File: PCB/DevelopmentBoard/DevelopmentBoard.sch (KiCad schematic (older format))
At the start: 27 parts, among them J2 Conn_01x04_MountingPin-Payloa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, J5 Conn_01x04_MountingPin, U1 D24V22F5_VoltageRegulator, U2 Barometer_Grove, U3 RASPBERRY_PI_3_MODEL_B+, U4 Conn_01x08_DevBoardSymbols, U6 MCP3008_ADC, U7 Conn_01x06_DevBoard_Symbols, X1 XT30, X2 XT30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

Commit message: Rewired I2C Pins on the Pi
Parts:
- gave numbers to parts that had none: 1
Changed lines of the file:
@@
 	5000 10000 9000 10000
 Wire Wire Line
+	7750 10850 8000 10850
+Wire Wire Line
 	7750 10750 8000 10750
-Wire Wire Line
-	7750 10850 8000 10850
+Text Label 8000 10850 2    50   ~ 0
+SDA
 Text Label 8000 10750 2    50   ~ 0
-SDA
-Text Label 8000 10850 2    50   ~ 0
 SCL
 $Comp
@@
 Text Label 1150 17900 1    50   ~ 0
 CS_ADC
-Text Label 1800 4350 0    50   ~ 0
+Text Label 1800 2550 0    50   ~ 0
 SCL
-Text Label 1800 4250 0    50   ~ 0
+Text Label 1800 2450 0    50   ~ 0
 SDA
 Wire Wire Line
-	1950 4350 1750 4350
-Wire Wire Line
-	1950 4250 1750 4250
+	1950 2550 1750 2550
+Wire Wire Line
+	1950 2450 1750 2450
 $Comp
 L power:+5V #PWR0116
@@
 $EndComp
 $Comp
-L Connector:TestPoint TP?
+L Connector:TestPoint TP2
 U 1 1 623429F1
 P 1100 15350
-F 0 "TP?" H 1158 15468 50  0000 L CNN
+F 0 "TP2" H 1158 15468 50  0000 L CNN
 F 1 "TestPoint" H 1158 15377 50  0000 L CNN
 F 2 "TestPoint:TestPoint_Pad_D2.5mm" H 1300 15350 50  0001 C CNN
@@
 $EndComp
 $Comp
-L power:+3V3 #PWR?
+L power:+3V3 #PWR0120
 U 1 1 623433B8
 P 1100 15350
-F 0 "#PWR?" H 1100 15200 50  0001 C CNN
+F 0 "#PWR0120" H 1100 15200 50  0001 C CNN
 F 1 "+3V3" H 1115 15523 50  0000 C CNN
 F 2 "" H 1100 15350 50  0001 C CNN

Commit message: Added I2C Outputs on the TBS Module
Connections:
- wire segments 60 -> 62
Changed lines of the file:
@@
 U 1 1 617175F8
 P 1600 15250
-F 0 "X1" H 1800 15350 50  0000 C CNN
-F 1 "XT30" H 1850 15250 50  0000 C CNN
+F 0 "X1" H 1900 15450 50  0000 C CNN
+F 1 "XT30" H 2000 15100 50  0000 C CNN
 F 2 "Connector_AMASS:AMASS_XT30U-M_1x02_P5.0mm_Vertical" H 1550 15250 50  0001 C CNN
 F 3 "" H 1550 15250 50  0001 C CNN
@@
 P 1100 15350
 F 0 "TP2" H 1158 15468 50  0000 L CNN
-F 1 "TestPoint" H 1158 15377 50  0000 L CNN
+F 1 "TestPoint" H 1150 15400 50  0000 L CNN
 F 2 "TestPoint:TestPoint_Pad_D2.5mm" H 1300 15350 50  0001 C CNN
 F 3 "~" H 1300 15350 50  0001 C CNN
@@
 	-1   0    0    1
 $EndComp
+Text Label 3450 15800 0    50   ~ 0
+SCL
+Text Label 3450 15700 0    50   ~ 0
+SDA
+Wire Wire Line
+	3600 15800 3400 15800
+Wire Wire Line
+	3600 15700 3400 15700
 $EndSCHEMATC

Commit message: FInal Tracing changes and Copper Refill.
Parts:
- renumbered R20 to R5
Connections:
- wire segments 62 -> 65
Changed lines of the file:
@@
 CS_ADC
 $Comp
-L Connector:TestPoint TP1
-U 1 1 626A437A
-P 2400 15250
-F 0 "TP1" H 2458 15368 50  0000 L CNN
-F 1 "TestPoint" H 2458 15277 50  0000 L CNN
-F 2 "TestPoint:TestPoint_Pad_D2.5mm" H 2600 15250 50  0001 C CNN
-F 3 "~" H 2600 15250 50  0001 C CNN
-	1    2400 15250
-	1    0    0    -1
-$EndComp
-$Comp
-L power:+12V #PWR0114
-U 1 1 626A5499
-P 2400 15250
-F 0 "#PWR0114" H 2400 15100 50  0001 C CNN
-F 1 "+12V" H 2415 15423 50  0000 C CNN
-F 2 "" H 2400 15250 50  0001 C CNN
-F 3 "" H 2400 15250 50  0001 C CNN
-	1    2400 15250
-	-1   0    0    1
-$EndComp
-$Comp
-L Device:R_Small_US R20
+L Device:R_Small_US R5
 U 1 1 626DE972
 P 1150 17100
-F 0 "R20" H 1218 17146 50  0000 L CNN
+F 0 "R5" H 1218 17146 50  0000 L CNN
 F 1 "4.7k" H 1218 17055 50  0000 L CNN
 F 2 "DevelopmentBoard:0603" H 1150 17100 50  0001 C CNN
@@
 Wire Wire Line
 	3600 15700 3400 15700
+$Comp
+L Connector:TestPoint TP1
+U 1 1 626A437A
+P 2400 15250
+F 0 "TP1" H 2458 15368 50  0000 L CNN
+F 1 "TestPoint" H 2458 15277 50  0000 L CNN
+F 2 "TestPoint:TestPoint_Pad_D2.5mm" H 2600 15250 50  0001 C CNN
+F 3 "~" H 2600 15250 50  0001 C CNN
+	1    2400 15250
+	1    0    0    -1
+$EndComp
+Wire Wire Line
+	2400 15250 2400 15400
+Wire Wire Line
+	2400 15400 2050 15400
+Wire Wire Line
+	2050 15400 2050 15700
+Connection ~ 2050 15700
 $EndSCHEMATC

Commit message: Added regulator symbols
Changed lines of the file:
@@
 	1000 22500 1000 1000
 Wire Notes Line
-	700  950  8700 950
+	1000 975  9000 975
 Wire Notes Line
 	9000 1000 9000 22500

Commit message: Added NAV route to breakout
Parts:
- added U?: VN-100_Breakout, symbol DevelopmentBoard:VN-100_Breakout
- R1, R11, R12, R13, R14, R15, R2, R3, R4, R5, R6: symbol Device:R_Small_US -> DevelopmentBoard-rescue:R_Small_US-Device
- TP1, TP2, TP3, TP4: symbol Connector:TestPoint -> DevelopmentBoard-rescue:TestPoint-Connector
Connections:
- net labels added: +5V-power, GND-power, NAV_RX, NAV_TX
- wire segments 65 -> 74
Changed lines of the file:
@@
 $EndDescr
 $Comp
-L power:GND #PWR0164
+L DevelopmentBoard-rescue:GND-power #PWR0164
 U 1 1 61619131
 P 4400 15500
@@
 $EndComp
 $Comp
-L power:+5V #PWR0165
+L DevelopmentBoard-rescue:+5V-power #PWR0165
 U 1 1 6161BA5A
 P 4400 15600
@@
 $EndComp
 $Comp
-L power:GND #PWR0166
+L DevelopmentBoard-rescue:GND-power #PWR0166
 U 1 1 61656710
 P 1850 15200
@@
 $EndComp
 $Comp
-L power:+12V #PWR0167
+L DevelopmentBoard-rescue:+12V-power #PWR0167
 U 1 1 61660D0C
 P 1850 15300
@@
 	1750 15300 1850 15300
 $Comp
-L power:GND #PWR0168
+L DevelopmentBoard-rescue:GND-power #PWR0168
 U 1 1 6161AEF3
 P 3600 15600
@@
 	3400 17300 3050 17300
 $Comp
-L power:GND #PWR0171
+L DevelopmentBoard-rescue:GND-power #PWR0171
 U 1 1 616717DD
 P 3400 17100
@@
 $EndComp
 $Comp
-L power:+5V #PWR0172
+L DevelopmentBoard-rescue:+5V-power #PWR0172
 U 1 1 6167029D
 P 3400 17200
@@
 $EndComp
 $Comp
-L power:+3.3V #PWR0177
+L DevelopmentBoard-rescue:+3.3V-power #PWR0177
 U 1 1 6160D985
 P 2000 17000
@@
 $EndComp
 $Comp
-L power:+3.3V #PWR0178
+L DevelopmentBoard-rescue:+3.3V-power #PWR0178
 U 1 1 6160D97F
 P 1600 17000
@@
 $EndComp
 $Comp
-L Device:R_Small_US R1
+L DevelopmentBoard-rescue:R_Small_US-Device R1
 U 1 1 6160D96F
 P 1600 17100
@@
 $EndComp
 $Comp
-L Device:R_Small_US R3
+L DevelopmentBoard-rescue:R_Small_US-Device R3
 U 1 1 6160D975
 P 2000 17100
@@
 SCL
 $Comp
-L power:+5V #PWR0208
+L DevelopmentBoard-rescue:+5V-power #PWR0208
 U 1 1 61DC74CC
 P 7750 10950
@@
 $EndComp
 $Comp
-L power:GND #PWR0207
+L DevelopmentBoard-rescue:GND-power #PWR0207
 U 1 1 61DC5E51
 P 7750 11050
@@
 	1750 15700 2050 15700
 $Comp
-L power:GND #PWR0101
+L DevelopmentBoard-rescue:GND-power #PWR0101
 U 1 1 6235DC57
 P 2200 15850
@@
 $EndComp
 $Comp
-L power:GND #PWR0102
+L DevelopmentBoard-rescue:GND-power #PWR0102
 U 1 1 6236A06D
 P 2200 15950
@@
 $EndComp
 $Comp
-L power:+5V #PWR0103
+L DevelopmentBoard-rescue:+5V-power #PWR0103
 U 1 1 62384BC7
 P 2250 16050
@@
 	7900 2550 8100 2550
 $Comp
-L power:GND #PWR0106
+L DevelopmentBoard-rescue:GND-power #PWR0106
 U 1 1 62490609
 P 8100 2550
@@
 $EndComp
 $Comp
-L power:GND #PWR0107
+L DevelopmentBoard-rescue:GND-power #PWR0107
 U 1 1 6249144C
 P 8250 3050
@@
 	1600 3650 1950 3650
 $Comp
-L Device:R_Small_US R2
+L DevelopmentBoard-rescue:R_Small_US-Device R2
 U 1 1 624B7DEB
 P 6650 2350
@@
 $EndComp
 $Comp
-L Device:R_Small_US R4
+L DevelopmentBoard-rescue:R_Small_US-Device R4
 U 1 1 624BB4C6
 P 6650 2450
@@
 $EndComp
 $Comp
-L Device:R_Small_US R6
+L DevelopmentBoard-rescue:R_Small_US-Device R6
 U 1 1 624BDAC4
 P 6650 2550
@@
 $EndComp
 $Comp
-L Device:R_Small_US R11
+L DevelopmentBoard-rescue:R_Small_US-Device R11
 U 1 1 624BE5AF
 P 6650 2650
@@
 $EndComp
 $Comp
-L Device:R_Small_US R12
+L DevelopmentBoard-rescue:R_Small_US-Device R12
 U 1 1 624BF3CC
 P 6650 2750
@@
 $EndComp
 $Comp
-L Device:R_Small_US R13
+L DevelopmentBoard-rescue:R_Small_US-Device R13
 U 1 1 624BFB63
 P 6650 2850
@@
 $EndComp
 $Comp
-L Device:R_Small_US R14
+L DevelopmentBoard-rescue:R_Small_US-Device R14
 U 1 1 624C06DD
 P 6650 2950
@@
 $EndComp
 $Comp
-L Device:R_Small_US R15
+L DevelopmentBoard-rescue:R_Small_US-Device R15
 U 1 1 624C10BC
 P 6650 3050
@@
 	6250 3050 6550 3050
 $Comp
-L Connector:TestPoint TP4
+L DevelopmentBoard-rescue:TestPoint-Connector TP4
 U 1 1 62563BD3
 P 1550 16050
@@
 $EndComp
 $Comp
-L power:+5V #PWR0108
+L DevelopmentBoard-rescue:+5V-power #PWR0108
 U 1 1 62568910
 P 1550 16050
@@
 $EndComp
 $Comp
-L Connector:TestPoint TP3
+L DevelopmentBoard-rescue:TestPoint-Connector TP3
 U 1 1 6256C309
 P 1100 16050
@@
 $EndComp
 $Comp
-L power:GND #PWR0109
+L DevelopmentBoard-rescue:GND-power #PWR0109
 U 1 1 6256D475
 P 1100 16050
@@
 	6200 11750 6400 11750
 $Comp
-L power:GND #PWR0110
+L DevelopmentBoard-rescue:GND-power #PWR0110
 U 1 1 62628D89
 P 6200 11950
@@
 $EndComp
 $Comp
-L power:+5V #PWR0111
+L DevelopmentBoard-rescue:+5V-power #PWR0111
 U 1 1 62629E2C
 P 6200 11850
@@
 $EndComp
 $Comp
-L power:+5V #PWR0112
+L DevelopmentBoard-rescue:+5V-power #PWR0112
 U 1 1 626358DD
 P 7850 12050
@@
 $EndComp
 $Comp
-L power:GND #PWR0113
+L DevelopmentBoard-rescue:GND-power #PWR0113
 U 1 1 6263718E
 P 7850 12150
@@
 CS_ADC
 $Comp
-L Device:R_Small_US R5
+L DevelopmentBoard-rescue:R_Small_US-Device R5
 U 1 1 626DE972
 P 1150 17100
@@
 $EndComp
 $Comp
-L power:+3.3V #PWR0115
+L DevelopmentBoard-rescue:+3.3V-power #PWR0115
 U 1 1 626DFEE0
 P 1150 17000
@@
 	1950 2450 1750 2450
 $Comp
-L power:+5V #PWR0116
+L DevelopmentBoard-rescue:+5V-power #PWR0116
 U 1 1 623DD84B
 P 4050 2350
@@
 $EndComp
 $Comp
-L power:+3.3V #PWR0117
+L DevelopmentBoard-rescue:+3.3V-power #PWR0117
 U 1 1 62402BAE
 P 4050 2450
@@
 	7900 2750 8250 2750
 $Comp
-L power:+5V #PWR0104
+L DevelopmentBoard-rescue:+5V-power #PWR0104
 U 1 1 6232D937
 P 8100 2350
@@
 $EndComp
 $Comp
-L power:+5V #PWR0105
+L DevelopmentBoard-rescue:+5V-power #PWR0105
 U 1 1 6232E513
 P 8100 2450
@@
 $EndComp
 $Comp
-L power:GND #PWR0118
+L DevelopmentBoard-rescue:GND-power #PWR0118
 U 1 1 62355844
 P 4050 4550
@@
 $EndComp
 $Comp
-L power:GND #PWR0119
+L DevelopmentBoard-rescue:GND-power #PWR0119
 U 1 1 62356241
 P 4050 4450
@@
 $EndComp
 $Comp
-L Connector:TestPoint TP2
+L DevelopmentBoard-rescue:TestPoint-Connector TP2
 U 1 1 623429F1
 P 1100 15350
@@
 $EndComp
 $Comp
-L power:+3V3 #PWR0120
+L DevelopmentBoard-rescue:+3V3-power #PWR0120
 U 1 1 623433B8
 P 1100 15350
@@
 	3600 15700 3400 15700
 $Comp
-L Connector:TestPoint TP1
+L DevelopmentBoard-rescue:TestPoint-Connector TP1
 U 1 1 626A437A
 P 2400 15250
@@
 	2050 15400 2050 15700
 Connection ~ 2050 15700
+$Comp
+L DevelopmentBoard:VN-100_Breakout U?
+U 1 1 625A78A9
+P 2950 9650
+F 0 "U?" H 2950 10415 50  0000 C CNN
+F 1 "VN-100_Breakout" H 2950 10324 50  0000 C CNN
+F 2 "" H 3000 9950 50  0001 C CNN
+F 3 "" H 3000 9950 50  0001 C CNN
+	1    2950 9650
+	1    0    0    -1
+$EndComp
+$Comp
+L DevelopmentBoard-rescue:+5V-power #PWR?
+U 1 1 625ABE16
+P 3650 9300
+F 0 "#PWR?" H 3650 9150 50  0001 C CNN
+F 1 "+5V-power" H 3665 9473 50  0000 C CNN
+F 2 "" H 3650 9300 50  0001 C CNN
+F 3 "" H 3650 9300 50  0001 C CNN
+	1    3650 9300
+	1    0    0    -1
+$EndComp
+Wire Wire Line
+	3400 9300 3650 9300
+$Comp
+L DevelopmentBoard-rescue:GND-power #PWR?
+U 1 1 625B8F57
+P 3400 10200
+F 0 "#PWR?" H 3400 9950 50  0001 C CNN
+F 1 "GND-power" H 3405 10027 50  0000 C CNN
+F 2 "" H 3400 10200 50  0001 C CNN
+F 3 "" H 3400 10200 50  0001 C CNN
+	1    3400 10200
+	1    0    0    -1
+$EndComp
+Wire Wire Line
+	3400 10050 3400 10200
+Connection ~ 3400 10200
+Wire Wire Line
+	2500 9450 2300 9450
+Text Label 2300 9450 0    50   ~ 0
+SCLK
+Wire Wire Line
+	2500 9600 2300 9600
+Text Label 2300 9600 0    50   ~ 0
+MOSI
+Wire Wire Line
+	2500 9750 2300 9750
+Text Label 2300 9750 0    50   ~ 0
+MISO
+Text Label 4350 2650 2    50   ~ 0
+NAV_RX
+Wire Wire Line
+	4050 2750 4350 2750
+Wire Wire Line
+	4050 2650 4350 2650
+Text Label 4350 2750 2    50   ~ 0
+NAV_TX
+Wire Wire Line
+	3400 9900 3700 9900
+Text Label 3700 9750 2    50   ~ 0
+NAV_TX
+Wire Wire Line
+	3400 9750 3700 9750
+Text Label 3700 9900 2    50   ~ 0
+NAV_RX
 $EndSCHEMATC

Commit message: initial board layout and traces
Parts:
- removed J2: Conn_01x04_MountingPin-PayloadSymbols, Connector_PinHeader_2.54mm:PinHeader_1x04_P2.54mm_Vertical, symbol DevelopmentBoard-rescue:Conn_01x04_MountingPin-PayloadSymbols
- removed R11, R12, R13, R14, R15, R2, R4, R6: 0, DevelopmentBoard:0603, symbol DevelopmentBoard-rescue:R_Small_US-Device
- removed R5: 4.7k, DevelopmentBoard:0603, symbol DevelopmentBoard-rescue:R_Small_US-Device
- removed U2: Barometer_Grove, DevelopmentBoard:Barometer_Grove, symbol DevelopmentBoard-rescue:Barometer_Grove-PayloadSymbols
- removed U6: MCP3008_ADC, DevelopmentBoard:MCP3008_ADC, symbol DevelopmentBoard:MCP3008_ADC
- removed X3: 2mmGrove_Connector, DevelopmentBoard:2mmGrove_Connector, symbol DevelopmentBoard:2mmGrove_Connector
- added R10, R11, R12, R2, R4, R5, R6, R7, R8, R9: 0, DevelopmentBoard:0603, symbol Device:R_Small_US
- U2: renamed from U?; footprint (none) -> DevelopmentBoard:VN-100Breakout
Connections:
- net labels added: SPI_CS
- net labels removed: CS_ADC
- wire segments 74 -> 56
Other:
- note added: "I2C Pullups"
- note removed: "ADC"
- note removed: "Altimeter"
- note removed: "SPI and I2C Pullups"
- note removed: "USB Controller"
- note removed: "USB Ports"
- moved on the sheet: J5

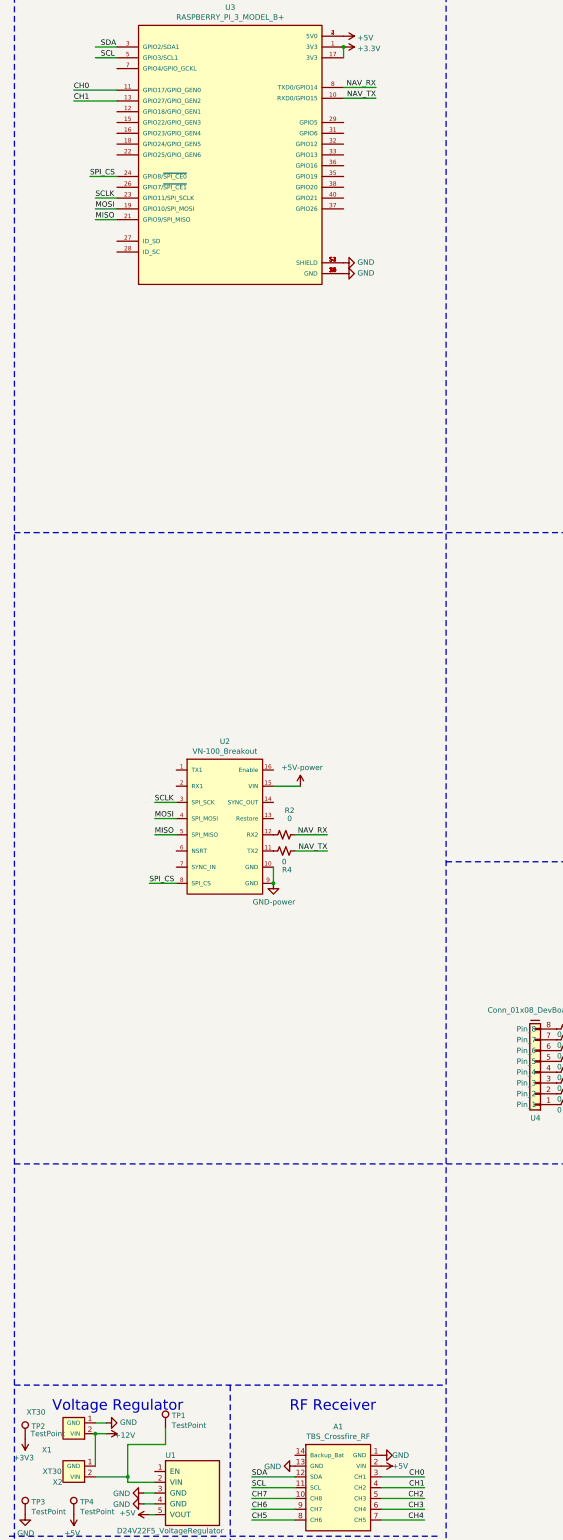
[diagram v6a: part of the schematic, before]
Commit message: Routed TBS connector
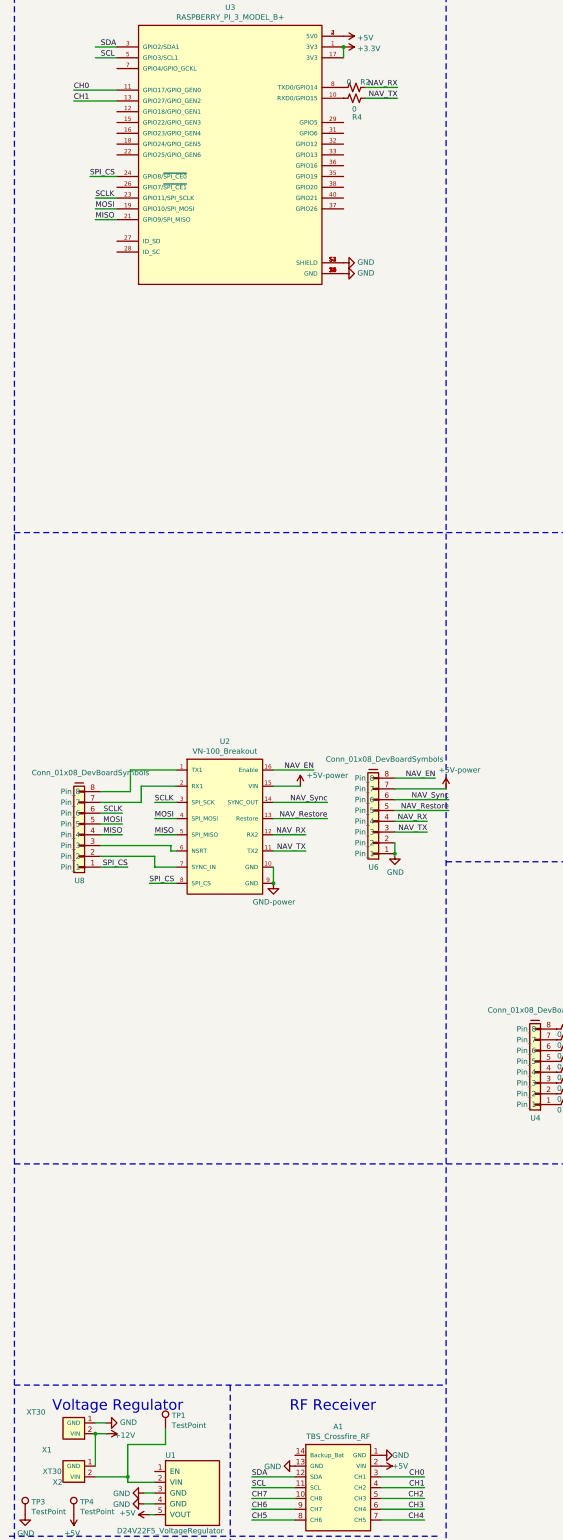
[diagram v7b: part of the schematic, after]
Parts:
- removed TP2: TestPoint, TestPoint:TestPoint_Pad_D2.5mm, symbol DevelopmentBoard-rescue:TestPoint-Connector
- added U6, U8: Conn_01x08_DevBoardSymbols, Connector_PinHeader_2.54mm:PinHeader_1x08_P2.54mm_Vertical, symbol DevelopmentBoard:Conn_01x08_DevBoardSymbols
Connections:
- net labels added: NAV_EN, NAV_Restore, NAV_Sync
- net labels removed: +3V3
- wire segments 56 -> 82
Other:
- moved on the sheet: R2, R4
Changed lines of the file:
@@
 	0    -1   -1   0
-$EndComp
-$Comp
-L DevelopmentBoard-rescue:TestPoint-Connector TP2
-U 1 1 623429F1
-P 1100 15350
-F 0 "TP2" H 1158 15468 50  0000 L CNN
-F 1 "TestPoint" H 1150 15400 50  0000 L CNN
-F 2 "TestPoint:TestPoint_Pad_D2.5mm" H 1300 15350 50  0001 C CNN
-F 3 "~" H 1300 15350 50  0001 C CNN
-	1    1100 15350
-	1    0    0    -1
-$EndComp
-$Comp
-L DevelopmentBoard-rescue:+3V3-power #PWR0120
-U 1 1 623433B8
-P 1100 15350
-F 0 "#PWR0120" H 1100 15200 50  0001 C CNN
-F 1 "+3V3" H 1115 15523 50  0000 C CNN
-F 2 "" H 1100 15350 50  0001 C CNN
-F 3 "" H 1100 15350 50  0001 C CNN
-	1    1100 15350
-	-1   0    0    1
 $EndComp
 Text Label 3200 15800 0    50   ~ 0
@@
 P 3650 9300
 F 0 "#PWR0104" H 3650 9150 50  0001 C CNN
-F 1 "+5V-power" H 3665 9473 50  0000 C CNN
+F 1 "+5V-power" H 3900 9400 50  0000 C CNN
 F 2 "" H 3650 9300 50  0001 C CNN
 F 3 "" H 3650 9300 50  0001 C CNN
@@
 Text Label 2300 9750 0    50   ~ 0
 MISO
-Text Label 3900 9900 2    50   ~ 0
+Text Label 3700 9900 2    50   ~ 0
 NAV_TX
 Wire Wire Line
-	3600 9900 3900 9900
-Wire Wire Line
-	3600 9750 3900 9750
-Text Label 3900 9750 2    50   ~ 0
+	3400 9900 3700 9900
+Wire Wire Line
+	3400 9750 3700 9750
+Text Label 3700 9750 2    50   ~ 0
 NAV_RX
 $Comp
@@
 Connection ~ 4050 2450
 Wire Wire Line
-	4050 2825 4350 2825
-Wire Wire Line
-	4050 2925 4350 2925
-Text Label 4350 2825 2    50   ~ 0
+	4250 2825 4550 2825
+Wire Wire Line
+	4250 2925 4550 2925
+Text Label 4550 2825 2    50   ~ 0
 NAV_RX
-Text Label 4350 2925 2    50   ~ 0
+Text Label 4550 2925 2    50   ~ 0
 NAV_TX
 Text Label 2250 10200 0    50   ~ 0
@@
 	1    5825 11650
 	-1   0    0    1
-$EndComp
-$Comp
-L Device:R_Small_US R2
-U 1 1 625FEBDD
-P 3500 9750
-F 0 "R2" V 3275 9800 50  0000 C CNN
-F 1 "0" V 3350 9800 50  0000 C CNN
-F 2 "DevelopmentBoard:0603" H 3500 9750 50  0001 C CNN
-F 3 "~" H 3500 9750 50  0001 C CNN
-	1    3500 9750
-	0    1    1    0
-$EndComp
-$Comp
-L Device:R_Small_US R4
-U 1 1 626003A3
-P 3500 9900
-F 0 "R4" V 3675 9925 50  0000 C CNN
-F 1 "0" V 3600 9900 50  0000 C CNN
-F 2 "DevelopmentBoard:0603" H 3500 9900 50  0001 C CNN
-F 3 "~" H 3500 9900 50  0001 C CNN
-	1    3500 9900
-	0    1    1    0
 $EndComp
 $Comp
@@
 Text Label 1550 2850 0    50   ~ 0
 CH0
+Text Label 4825 9625 2    50   ~ 0
+NAV_RX
+Wire Wire Line
+	4525 9625 4825 9625
+Text Label 4825 9725 2    50   ~ 0
+NAV_TX
+Connection ~ 4525 9925
+Wire Wire Line
+	4525 9825 4525 9925
+$Comp
+L power:GND #PWR0114
+U 1 1 6293F1F2
+P 4525 9925
+F 0 "#PWR0114" H 4525 9675 50  0001 C CNN
+F 1 "GND" H 4530 9752 50  0000 C CNN
+F 2 "" H 4525 9925 50  0001 C CNN
+F 3 "" H 4525 9925 50  0001 C CNN
+	1    4525 9925
+	1    0    0    -1
+$EndComp
+$Comp
+L DevelopmentBoard:Conn_01x08_DevBoardSymbols U6
+U 1 1 6293845E
+P 4325 9325
+F 0 "U6" H 4275 10050 50  0000 L CNN
+F 1 "Conn_01x08_DevBoardSymbols" H 3675 9050 50  0000 L CNN
+F 2 "Connector_PinHeader_2.54mm:PinHeader_1x08_P2.54mm_Vertical" H 4325 9775 50  0001 C CNN
+F 3 "" H 4325 9775 50  0001 C CNN
+	1    4325 9325
+	-1   0    0    1
+$EndComp
+$Comp
+L DevelopmentBoard-rescue:+5V-power #PWR0115
+U 1 1 629499D4
+P 5000 9325
+F 0 "#PWR0115" H 5000 9175 50  0001 C CNN
+F 1 "+5V-power" H 5125 9500 50  0000 C CNN
+F 2 "" H 5000 9325 50  0001 C CNN
+F 3 "" H 5000 9325 50  0001 C CNN
+	1    5000 9325
+	1    0    0    -1
+$EndComp
+Wire Wire Line
+	3400 9600 3900 9600
+Text Label 3900 9600 2    50   ~ 0
+NAV_Restore
+Wire Wire Line
+	3400 9450 3900 9450
+Text Label 3900 9450 2    50   ~ 0
+NAV_Sync
+Text Label 3775 9150 2    50   ~ 0
+NAV_EN
+Wire Wire Line
+	3400 9150 3775 9150
+Wire Wire Line
+	4525 9325 5000 9325
+Text Label 4900 9225 2    50   ~ 0
+NAV_EN
+Wire Wire Line
+	4525 9225 4900 9225
+Wire Wire Line
+	4525 9525 5025 9525
+Text Label 5025 9525 2    50   ~ 0
+NAV_Restore
+Wire Wire Line
+	4525 9425 5025 9425
+Text Label 5025 9425 2    50   ~ 0
+NAV_Sync
+Wire Wire Line
+	4525 9725 4825 9725
+$Comp
+L Device:R_Small_US R4
+U 1 1 626003A3
+P 4150 2925
+F 0 "R4" V 4325 2950 50  0000 C CNN
+F 1 "0" V 4250 2925 50  0000 C CNN
+F 2 "DevelopmentBoard:0603" H 4150 2925 50  0001 C CNN
+F 3 "~" H 4150 2925 50  0001 C CNN
+	1    4150 2925
+	0    1    1    0
+$EndComp
+$Comp
+L Device:R_Small_US R2
+U 1 1 625FEBDD
+P 4150 2825
+F 0 "R2" V 4100 2925 50  0000 C CNN
+F 1 "0" V 4100 2775 50  0000 C CNN
+F 2 "DevelopmentBoard:0603" H 4150 2825 50  0001 C CNN
+F 3 "~" H 4150 2825 50  0001 C CNN
+	1    4150 2825
+	0    1    1    0
+$EndComp
+$Comp
+L DevelopmentBoard:Conn_01x08_DevBoardSymbols U8
+U 1 1 629ABDFA
+P 1600 9450
+F 0 "U8" H 1550 10175 50  0000 L CNN
+F 1 "Conn_01x08_DevBoardSymbols" H 950 9175 50  0000 L CNN
+F 2 "Connector_PinHeader_2.54mm:PinHeader_1x08_P2.54mm_Vertical" H 1600 9900 50  0001 C CNN
+F 3 "" H 1600 9900 50  0001 C CNN
+	1    1600 9450
+	-1   0    0    1
+$EndComp
+Wire Wire Line
+	2000 9550 1800 9550
+Text Label 2000 9550 2    50   ~ 0
+SCLK
+Wire Wire Line
+	2000 9650 1800 9650
+Text Label 2000 9650 2    50   ~ 0
+MOSI
+Wire Wire Line
+	2000 9750 1800 9750
+Text Label 2000 9750 2    50   ~ 0
+MISO
+Text Label 2050 10050 2    50   ~ 0
+SPI_CS
+Wire Wire Line
+	1800 10050 2050 10050
+Wire Wire Line
+	1800 9350 2075 9350
+Wire Wire Line
+	2075 9350 2075 9150
+Wire Wire Line
+	2075 9150 2500 9150
+Wire Wire Line
+	1800 9450 2175 9450
+Wire Wire Line
+	2175 9450 2175 9300
+Wire Wire Line
+	2175 9300 2500 9300
+Wire Wire Line
+	1800 9850 2450 9850
+Wire Wire Line
+	2450 9850 2450 9900
+Wire Wire Line
+	2450 9900 2500 9900
+Wire Wire Line
+	1800 9950 2300 9950
+Wire Wire Line
+	2300 9950 2300 10050
+Wire Wire Line
+	2300 10050 2500 10050
 $EndSCHEMATC
